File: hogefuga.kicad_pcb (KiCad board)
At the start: 2 copper layers, 95.3 x 97.6 mm, 45 parts, among them J1 MJ-4PP-9, SW1 SW_PUSH, SW10 SW_PUSH, SW11 SW_PUSH, SW12 SW_PUSH, SW13 SW_PUSH, SW14 SW_PUSH, SW15 SW_PUSH, SW16 SW_PUSH, SW17 SW_PUSH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

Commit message: rev0.2
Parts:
- removed the Ref** at (133.3, 66.7)
- removed the Ref** at (133.3, 104.8)
- removed the Ref** at (76.2, 104.8)
- removed the Ref** at (76.2, 66.7)
- added Ref**: Val**, kbd:HOLE, F.Cu at (131.0, 78.6)
- added Ref**: Val**, kbd:HOLE, F.Cu at (131.0, 116.7)
- added Ref**: Val**, kbd:HOLE, F.Cu at (73.8, 116.7)
- added Ref**: Val**, kbd:HOLE, F.Cu at (73.8, 78.6)
- SW1, SW10, SW11, SW12, SW13, SW14, SW15, SW2, SW3, SW4, SW5, SW6, SW7, SW8, SW9: footprint lib:SW_Matias_1.00u -> keyboard_parts:ALPS_SKCM
- moved D17 20.5 mm to (100.0, 126.2)
- moved SW20 14.2 mm to (102.4, 45.2)
- moved D5 12.2 mm to (140.3, 78.6), turned to 0 degrees
- moved D13 12.1 mm to (102.4, 116.7), turned to 0 degrees
- moved D19 12.1 mm to (126.2, 126.2)
- moved D3 12.1 mm to (102.4, 78.6), turned to 0 degrees
- moved D8 12.1 mm to (102.4, 97.6), turned to 0 degrees
- moved D9 12.1 mm to (121.4, 97.6), turned to 0 degrees
- moved SW1 12.1 mm to (64.3, 69.1)
- moved SW10 12.1 mm to (140.5, 88.1)
- moved SW16 12.1 mm to (66.7, 126.2)
- moved SW17 12.1 mm to (90.5, 126.2)
- moved SW18 12.1 mm to (114.3, 126.2)
- moved SW2 12.1 mm to (83.3, 69.1)
- moved SW3 12.1 mm to (102.4, 69.1)
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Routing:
- net GND: track 161.6 -> 97.3 mm
- net col3: track 149.4 -> 86.6 mm
- net col5: track 155.2 -> 121.6 mm
- net col2: track 146.1 -> 120.1 mm
- net col4: track 136.6 -> 113.8 mm
- net row1: track 193.0 -> 173.5 mm
- net VCC: track 69.6 -> 54.2 mm
- net row2: track 228.7 -> 243.0 mm
- net data: track 60.1 -> 74.3 mm
- net col1: track 124.2 -> 111.8 mm
- net row0: track 167.0 -> 157.3 mm
- net Net-(D17-Pad2): track 19.6 -> 11.3 mm
- net Net-(D18-Pad2): track 21.9 -> 18.6 mm
- net row3: track 213.4 -> 215.8 mm
- net Net-(D16-Pad2): track 11.3 -> 13.7 mm
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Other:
- outline, holes or cut-outs redrawn
- board text added: "hogefuga keyboard v0.2 by yswallow"
- board text removed: "hogefuga v0.1 by yswallow"

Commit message: PCBを直接ボトムプレートに固定する穴を追加
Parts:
- added REF**: MountingHole_2.2mm_M2, MountingHole:MountingHole_2.2mm_M2, F.Cu at (147.6, 40.5)
- added REF**: MountingHole_2.2mm_M2, MountingHole:MountingHole_2.2mm_M2, F.Cu at (131.0, 97.6)
- added REF**: MountingHole_2.2mm_M2, MountingHole:MountingHole_2.2mm_M2, F.Cu at (73.8, 97.6)
- added REF**: MountingHole_2.2mm_M2, MountingHole:MountingHole_2.2mm_M2, F.Cu at (57.1, 40.5)
- added REF**: MountingHole_2.2mm_M2, MountingHole:MountingHole_2.2mm_M2, F.Cu at (57.1, 133.3)
- added REF**: MountingHole_2.2mm_M2, MountingHole:MountingHole_2.2mm_M2, F.Cu at (147.6, 133.3)
- added REF**: MountingHole_2.2mm_M2, MountingHole:MountingHole_2.2mm_M2, F.Cu at (131.0, 59.5)
- added REF**: MountingHole_2.2mm_M2, MountingHole:MountingHole_2.2mm_M2, F.Cu at (73.8, 59.5)
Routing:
- net row2: track 243.0 -> 241.3 mm
- net row3: track 215.8 -> 215.2 mm

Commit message: move TRRS jack
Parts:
- moved J1 5.32 mm to (111.9, 40.5)
- moved SW20 0.17 mm to (102.2, 45.2)
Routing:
- net row0: track 157.3 -> 202.7 mm
- net GND: track 97.3 -> 115.3 mm
- net data: track 74.3 -> 67.7 mm
- net col1: track 111.8 -> 110.6 mm
- net VCC: track 54.2 -> 53.3 mm

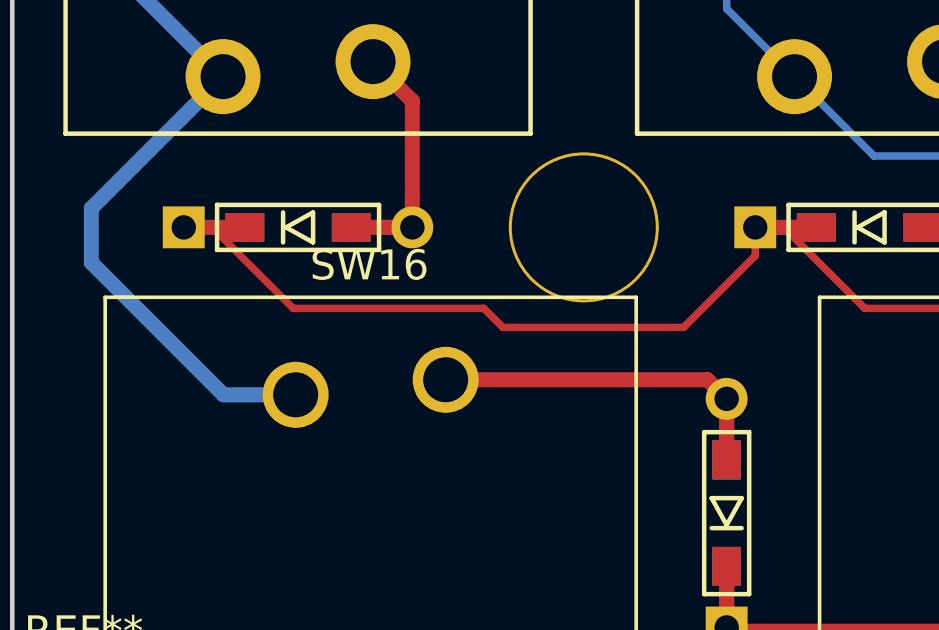
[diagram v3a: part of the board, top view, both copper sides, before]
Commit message: 配線の軽微な変更
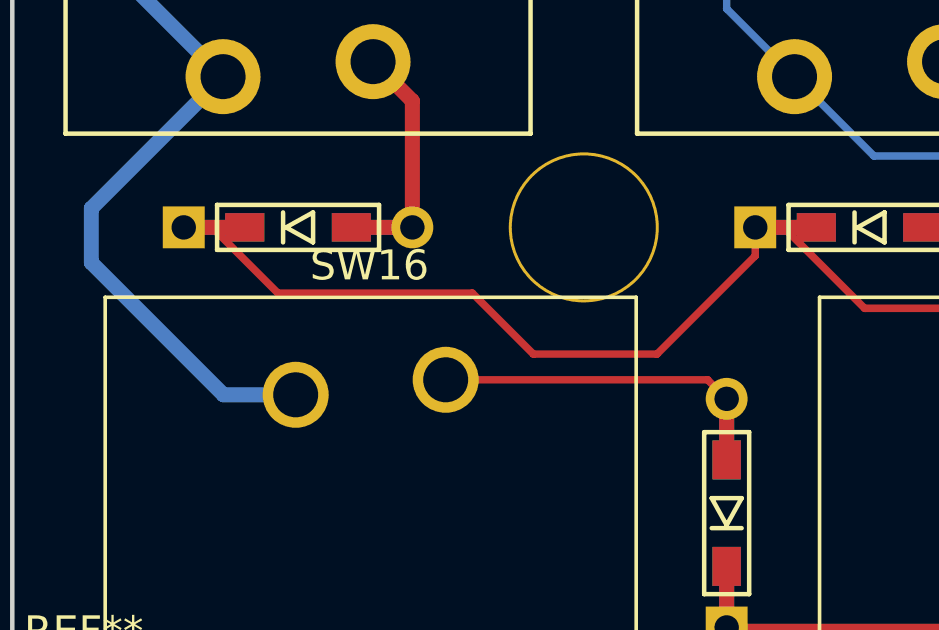
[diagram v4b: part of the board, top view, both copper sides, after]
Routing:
- net row2: track 241.2 -> 241.9 mm
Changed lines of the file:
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@@
   )
   (setup
-    (last_trace_width 0.5)
+    (last_trace_width 0.25)
     (user_trace_width 0.5)
     (trace_clearance 0.2)
@@
   (segment (start 80.48225 116.68125) (end 79.53375 116.68125) (width 0.25) (layer F.Cu) (net 13))
   (segment (start 96.8335 119.38) (end 83.181 119.38) (width 0.25) (layer F.Cu) (net 13))
-  (segment (start 79.53375 117.62975) (end 77.1485 120.015) (width 0.25) (layer F.Cu) (net 13))
-  (segment (start 79.53375 116.68125) (end 79.53375 117.62975) (width 0.25) (layer F.Cu) (net 13))
-  (segment (start 77.1485 120.015) (end 71.12 120.015) (width 0.25) (layer F.Cu) (net 13))
-  (segment (start 71.12 120.015) (end 70.485 119.38) (width 0.25) (layer F.Cu) (net 13))
-  (segment (start 61.43225 116.68125) (end 60.48375 116.68125) (width 0.25) (layer F.Cu) (net 13))
-  (segment (start 64.131 119.38) (end 61.43225 116.68125) (width 0.25) (layer F.Cu) (net 13))
-  (segment (start 70.485 119.38) (end 64.131 119.38) (width 0.25) (layer F.Cu) (net 13))
   (segment (start 60.48375 116.68125) (end 62.51875 116.68125) (width 0.5) (layer F.Cu) (net 13))
   (segment (start 81.56875 116.68125) (end 79.53375 116.68125) (width 0.5) (layer F.Cu) (net 13))
@@
   (segment (start 146.685 118.745) (end 146.685 69.85) (width 0.25) (layer F.Cu) (net 13))
   (segment (start 146.685 69.85) (end 142.39875 65.56375) (width 0.25) (layer F.Cu) (net 13))
+  (segment (start 79.53375 117.62975) (end 79.53375 116.68125) (width 0.25) (layer F.Cu) (net 13))
+  (segment (start 60.48375 116.68125) (end 61.43225 116.68125) (width 0.25) (layer F.Cu) (net 13))
+  (segment (start 63.623 118.872) (end 70.104 118.872) (width 0.25) (layer F.Cu) (net 13))
+  (segment (start 76.2595 120.904) (end 79.53375 117.62975) (width 0.25) (layer F.Cu) (net 13))
+  (segment (start 70.104 118.872) (end 72.136 120.904) (width 0.25) (layer F.Cu) (net 13))
+  (segment (start 61.43225 116.68125) (end 63.623 118.872) (width 0.25) (layer F.Cu) (net 13))
+  (segment (start 72.136 120.904) (end 76.2595 120.904) (width 0.25) (layer F.Cu) (net 13))
   (segment (start 66.06875 116.68125) (end 68.10375 116.68125) (width 0.5) (layer F.Cu) (net 14))
   (segment (start 68.10375 112.46625) (end 68.10375 116.68125) (width 0.5) (layer F.Cu) (net 14))
@@
   (segment (start 144.65 116.68125) (end 142.615 116.68125) (width 0.5) (layer F.Cu) (net 18))
   (segment (start 142.615 116.68125) (end 144.65 116.68125) (width 0.5) (layer B.Cu) (net 18))
-  (segment (start 77.94625 121.76125) (end 78.58125 122.39625) (width 0.5) (layer F.Cu) (net 19))
-  (segment (start 69.215 121.76125) (end 77.94625 121.76125) (width 0.5) (layer F.Cu) (net 19))
   (segment (start 78.58125 122.39625) (end 78.58125 124.43125) (width 0.5) (layer F.Cu) (net 19))
   (segment (start 78.58125 124.43125) (end 78.58125 122.39625) (width 0.5) (layer B.Cu) (net 19))
+  (segment (start 77.94625 121.76125) (end 78.58125 122.39625) (width 0.25) (layer F.Cu) (net 19))
+  (segment (start 69.215 121.76125) (end 77.94625 121.76125) (width 0.25) (layer F.Cu) (net 19))
   (segment (start 78.58125 127.98125) (end 78.58125 130.01625) (width 0.5) (layer F.Cu) (net 20))
   (segment (start 100.0125 130.01625) (end 100.0125 127.98125) (width 0.5) (layer F.Cu) (net 20))

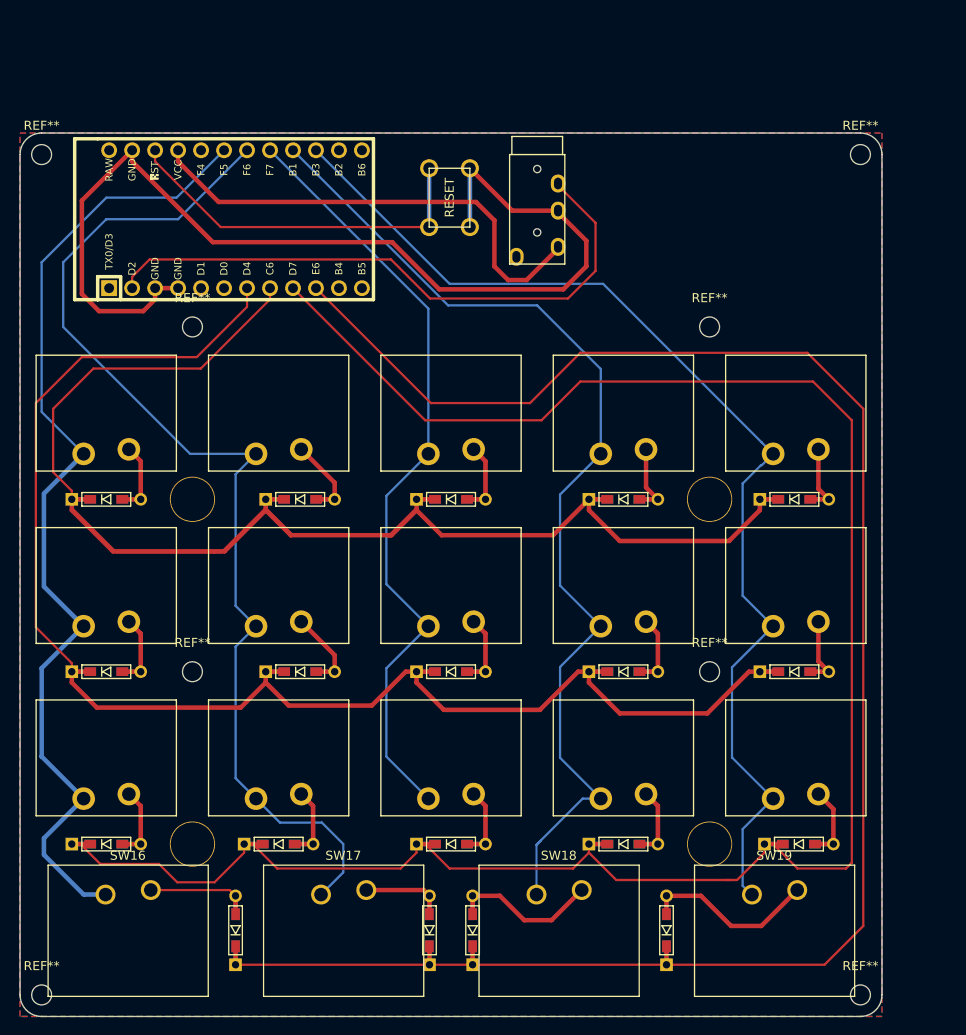
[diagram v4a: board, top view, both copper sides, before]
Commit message: スイッチを全てtmkさんのフットプリントに変更
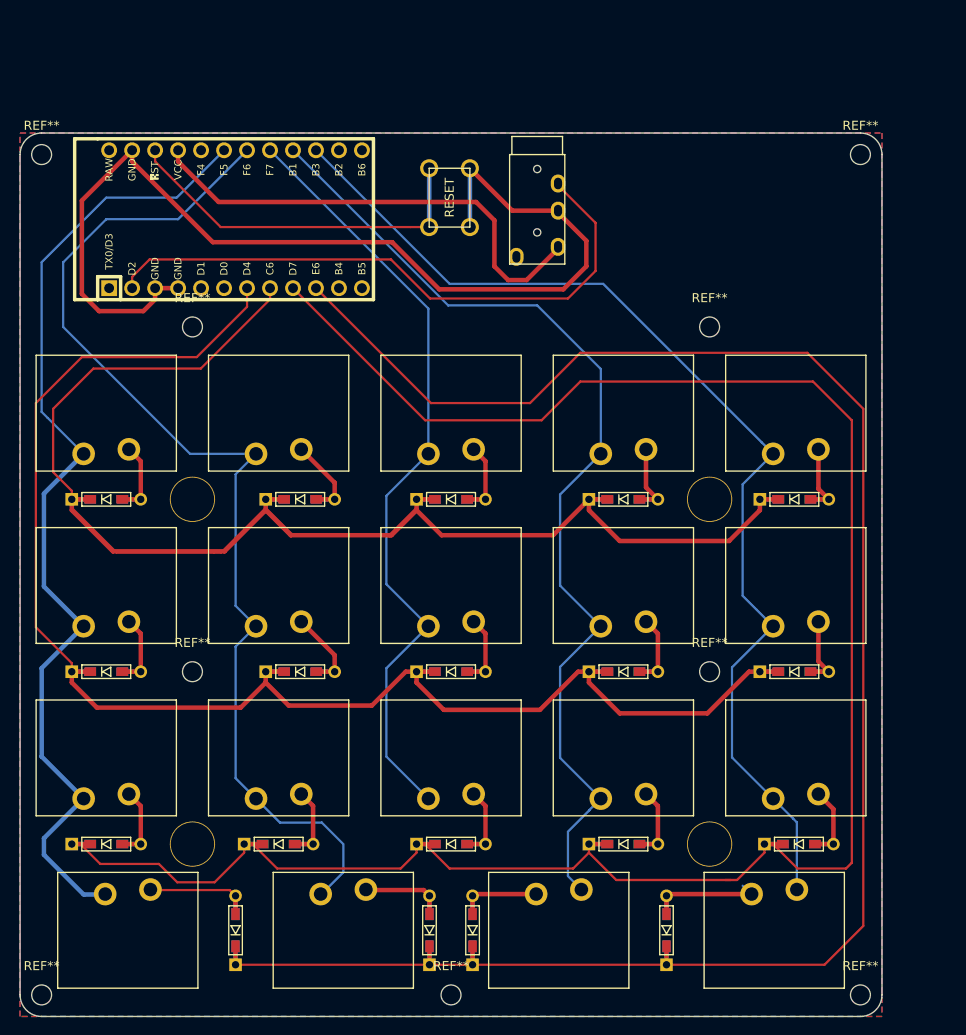
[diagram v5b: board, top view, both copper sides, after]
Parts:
- added REF**: MountingHole_2.2mm_M2, MountingHole:MountingHole_2.2mm_M2, F.Cu at (102.4, 133.3)
- SW16, SW17, SW18, SW19: footprint lib:SW_Matias_1.25u -> keyboard_parts:ALPS_SKCM
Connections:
- SW16 pad 1: Net-(D16-Pad2) -> col1
- SW16 pad 2: col1 -> Net-(D16-Pad2)
- SW17 pad 1: Net-(D17-Pad2) -> col2
- SW17 pad 2: col2 -> Net-(D17-Pad2)
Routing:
- net Net-(D18-Pad2): track 18.6 -> 11.2 mm
- net Net-(D19-Pad2): track 21.5 -> 15.0 mm
- net col4: track 114.2 -> 111.1 mm
- net col5: track 121.6 -> 120.2 mm

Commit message: プレートからボトムへのネジを追加
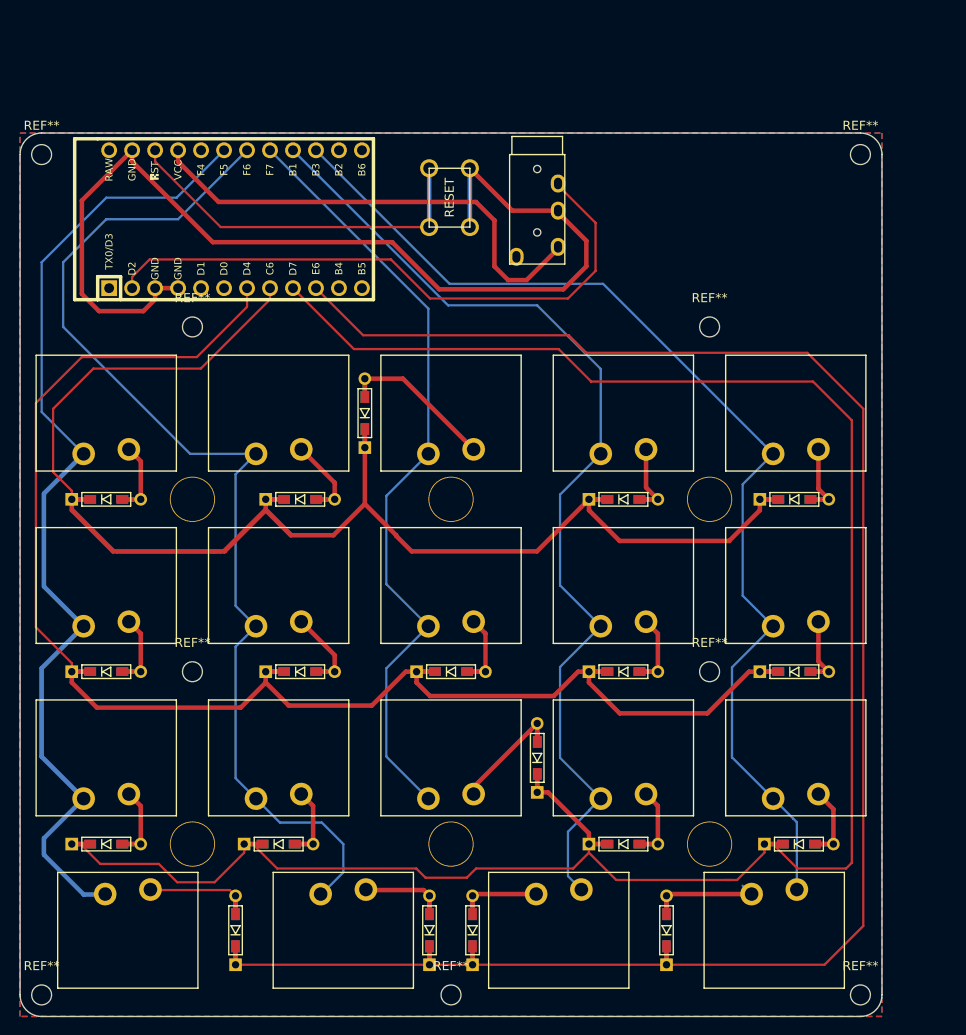
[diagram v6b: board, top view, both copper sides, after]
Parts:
- added Ref**: Val**, kbd:HOLE, F.Cu at (102.4, 116.7)
- added Ref**: Val**, kbd:HOLE, F.Cu at (102.4, 78.6)
- moved D13 13.5 mm to (111.9, 107.2), turned to 90 degrees
- moved D3 13.5 mm to (92.9, 69.1), turned to 90 degrees
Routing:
- net Net-(D3-Pad2): track 10.1 -> 19.3 mm
- net row0: track 202.7 -> 193.9 mm
- net Net-(D13-Pad2): track 10.1 -> 14.8 mm
- net row3: track 215.2 -> 210.6 mm
- net row2: track 241.9 -> 245.2 mm
- net row1: track 173.5 -> 172.3 mm
